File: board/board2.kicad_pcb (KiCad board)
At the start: 4 copper layers, 56 x 64 mm, 88 parts, among them J1 Battery, J2 Serial, J3 SWD, J4 Range_Front, J5 Range_Left, J6 Range_Right, J7 POWER, J8 EXP, SW1 RST, SW2 Left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

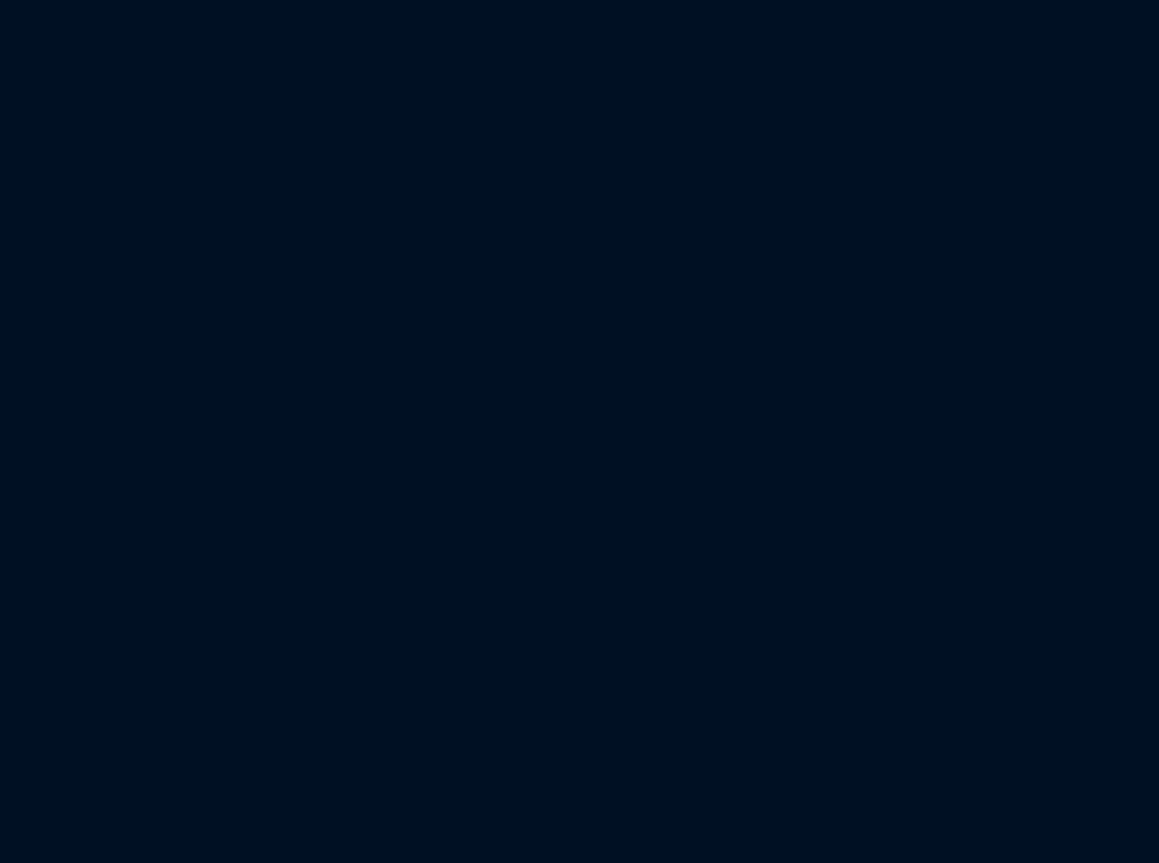
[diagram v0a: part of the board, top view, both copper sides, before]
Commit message: New board outline
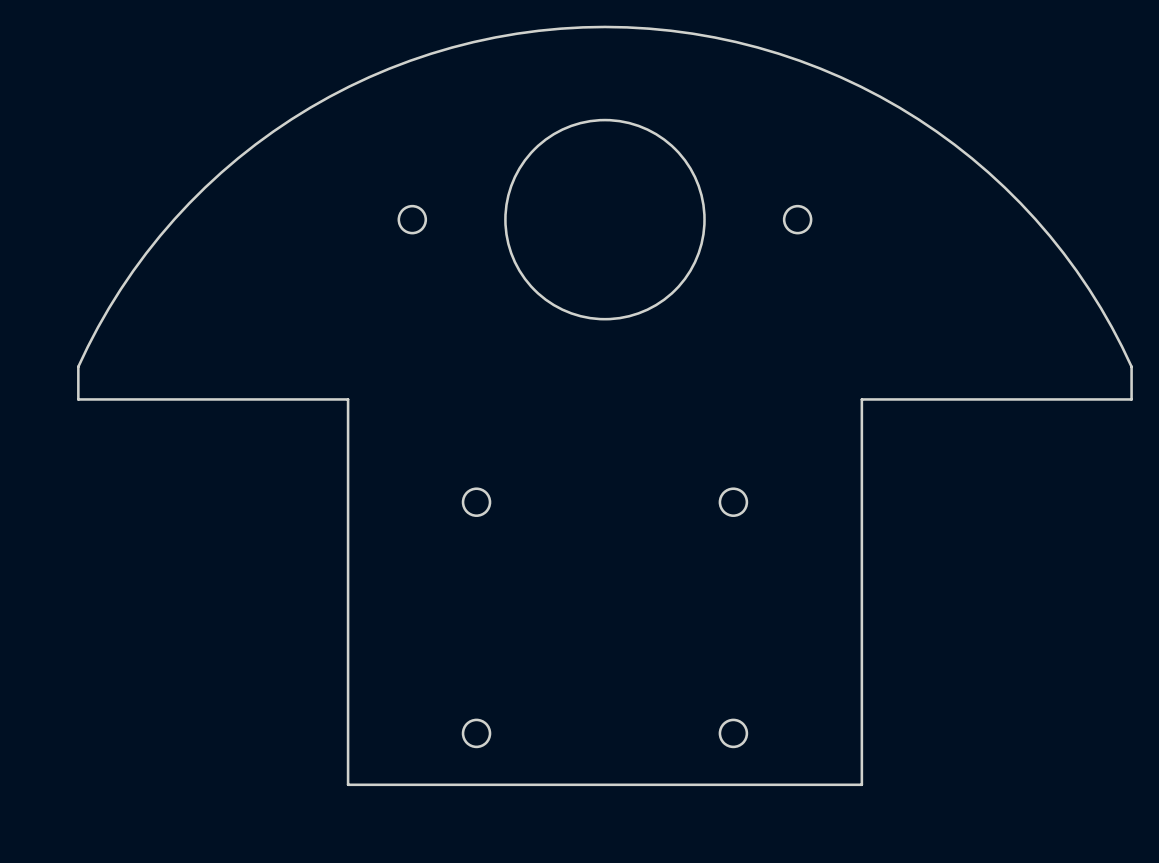
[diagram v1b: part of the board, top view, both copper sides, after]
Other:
- board size 56 x 64 mm -> 177 x 91 mm
